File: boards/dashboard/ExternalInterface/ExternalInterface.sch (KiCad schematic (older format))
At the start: 4 parts, among them J1 micromatch_female_TOP_ENTRY_l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, J2 Ampseal_14, J3 micromatch_female_TOP_ENTRY_l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, U1 RJ45_VT

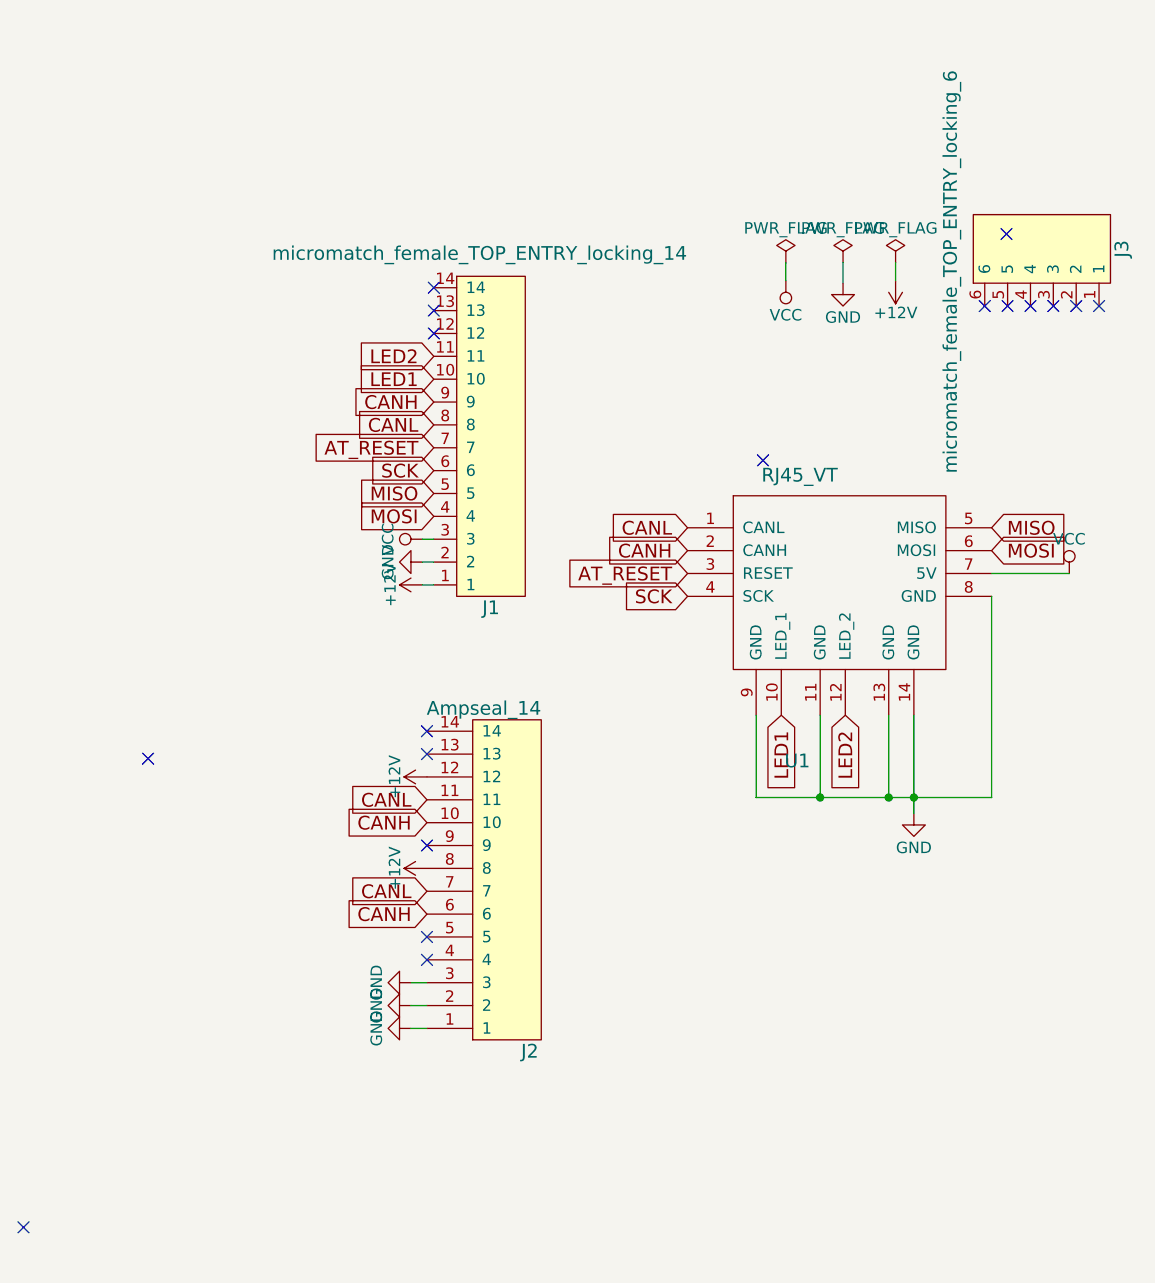
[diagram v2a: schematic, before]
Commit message: Updated External Interface
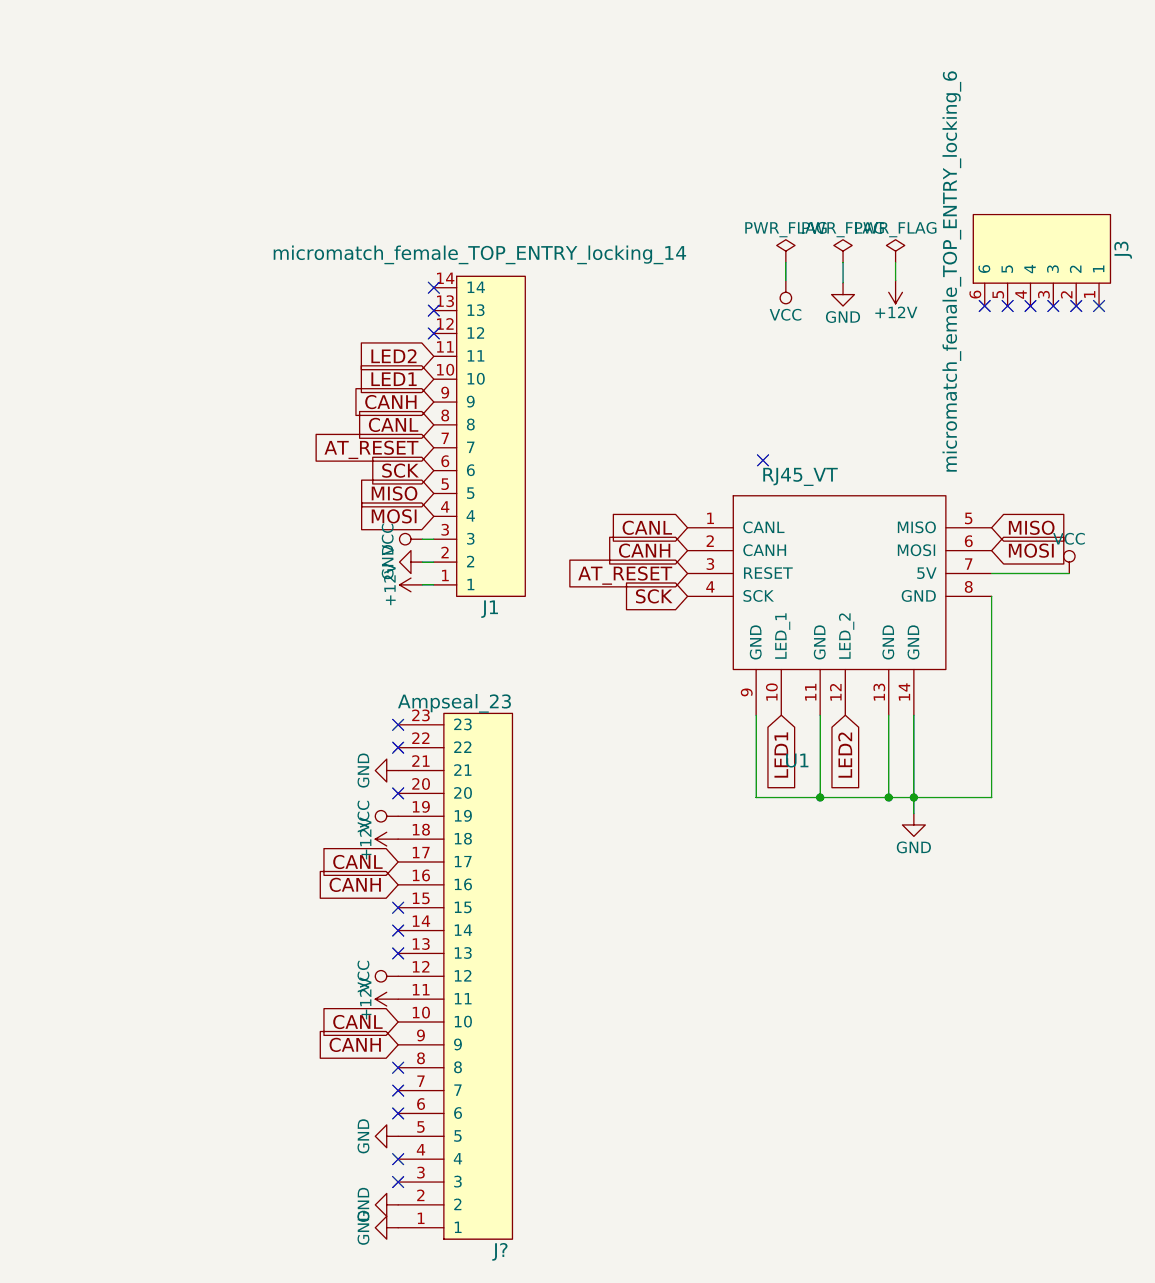
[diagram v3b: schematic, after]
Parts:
- removed J2: Ampseal_14, footprints:Ampseal_14, symbol Ampseal_14
- added J?: Ampseal_23, symbol Ampseal_23
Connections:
- net +12V: now also J?.11, J?.18
- net CANH: now also J?.16, J?.9
- net CANL: now also J?.10, J?.17
- net GND: now also J?.1, J?.2, J?.21, J?.5
- net VCC: now also J?.12, J?.19
- no-connect marks 18 -> 21
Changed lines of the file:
@@
-$EndComp
-$Comp
-L Ampseal_14 J2
-U 1 1 5A64D29C
-P 2180 4340
-F 0 "J2" H 1930 5090 60  0000 C CNN
-F 1 "Ampseal_14" H 1880 3590 60  0000 L CNN
-F 2 "footprints:Ampseal_14" H 1980 4640 60  0001 C CNN
-F 3 "" H 1980 4640 60  0001 C CNN
-	1    2180 4340
-	-1   0    0    1
-$EndComp
-$Comp
-L +12V #PWR010
-U 1 1 5A66323E
-P 1980 4290
-F 0 "#PWR010" H 1980 4140 50  0001 C CNN
-F 1 "+12V" H 1980 4430 50  0000 C CNN
-F 2 "" H 1980 4290 50  0001 C CNN
-F 3 "" H 1980 4290 50  0001 C CNN
-	1    1980 4290
-	0    -1   -1   0
-$EndComp
-Text GLabel 1980 4090 0    60   Input ~ 0
-CANH
-Text GLabel 1980 4490 0    60   Input ~ 0
-CANH
-Text GLabel 1980 3990 0    60   Input ~ 0
-CANL
-Text GLabel 1980 4390 0    60   Input ~ 0
-CANL
-$Comp
-L GND #PWR011
-U 1 1 5A663282
-P 1910 4790
-F 0 "#PWR011" H 1910 4540 50  0001 C CNN
-F 1 "GND" H 1910 4640 50  0000 C CNN
-F 2 "" H 1910 4790 50  0001 C CNN
-F 3 "" H 1910 4790 50  0001 C CNN
-	1    1910 4790
-	0    1    1    0
-$EndComp
-$Comp
-L GND #PWR012
-U 1 1 5A663293
-P 1910 4990
-F 0 "#PWR012" H 1910 4740 50  0001 C CNN
-F 1 "GND" H 1910 4840 50  0000 C CNN
-F 2 "" H 1910 4990 50  0001 C CNN
-F 3 "" H 1910 4990 50  0001 C CNN
-	1    1910 4990
-	0    1    1    0
 $EndComp
 $Comp
@@
 	1    0    0    -1
 $EndComp
-Wire Wire Line
-	2010 2950 1960 2950
-Wire Wire Line
-	2010 2850 1960 2850
-Wire Wire Line
-	2010 3050 1960 3050
-Wire Wire Line
-	3550 1640 3550 1720
-Wire Wire Line
-	3800 1640 3800 1730
-Wire Wire Line
-	4030 1640 4030 1720
-Wire Wire Line
-	1910 4790 1980 4790
-Wire Wire Line
-	1910 4890 1980 4890
-Wire Wire Line
-	1910 4990 1980 4990
 Text GLabel 4450 2800 2    60   Input ~ 0
 MISO
@@
 	1    0    0    -1
 $EndComp
-Wire Wire Line
-	4110 4050 4110 3620
-Wire Wire Line
-	4000 3620 4000 3980
-Wire Wire Line
-	3420 3980 4450 3980
-Connection ~ 4110 3980
-Wire Wire Line
-	3700 3620 3700 3980
-Connection ~ 4000 3980
-Wire Wire Line
-	3420 3620 3420 3980
-Connection ~ 3700 3980
-Wire Wire Line
-	4450 3980 4450 3100
 $Comp
 L VCC #PWR014
@@
 	1    0    0    -1
 $EndComp
-Wire Wire Line
-	4450 3000 4790 3000
 NoConn ~ 2010 1750
 NoConn ~ 2010 1850
@@
 NoConn ~ 4520 1830
 NoConn ~ 4420 1830
-$Comp
-L GND #PWR015
-U 1 1 5A8B7071
-P 1910 4890
-F 0 "#PWR015" H 1910 4640 50  0001 C CNN
-F 1 "GND" H 1910 4740 50  0000 C CNN
-F 2 "" H 1910 4890 50  0001 C CNN
-F 3 "" H 1910 4890 50  0001 C CNN
-	1    1910 4890
-	0    1    1    0
-$EndComp
-$Comp
-L +12V #PWR016
-U 1 1 5A8B721D
-P 1980 3890
-F 0 "#PWR016" H 1980 3740 50  0001 C CNN
-F 1 "+12V" H 1980 4030 50  0000 C CNN
-F 2 "" H 1980 3890 50  0001 C CNN
-F 3 "" H 1980 3890 50  0001 C CNN
-	1    1980 3890
-	0    -1   -1   0
-$EndComp
-NoConn ~ 1980 3790
-NoConn ~ 1980 3690
-NoConn ~ 1980 4190
-NoConn ~ 1980 4690
-NoConn ~ 1980 4590
 NoConn ~ 3450 2505
-NoConn ~ 215  5860
-NoConn ~ 760  3810
-NoConn ~ 4515 1515
+$Comp
+L Ampseal_23 J?
+U 1 1 5AA40700
+P 2054 4762
+F 0 "J?" H 1804 5962 60  0000 C CNN
+F 1 "Ampseal_23" H 1754 3562 60  0000 L CNN
+F 2 "" H 1854 5512 60  0001 C CNN
+F 3 "" H 1854 5512 60  0001 C CNN
+	1    2054 4762
+	-1   0    0    1
+$EndComp
+$Comp
+L GND #PWR?
+U 1 1 5AA408D9
+P 1854 5862
+F 0 "#PWR?" H 1854 5612 50  0001 C CNN
+F 1 "GND" H 1854 5712 50  0000 C CNN
+F 2 "" H 1854 5862 50  0001 C CNN
+F 3 "" H 1854 5862 50  0001 C CNN
+	1    1854 5862
+	0    1    1    0
+$EndComp
+$Comp
+L GND #PWR?
+U 1 1 5AA408F3
+P 1854 5762
+F 0 "#PWR?" H 1854 5512 50  0001 C CNN
+F 1 "GND" H 1854 5612 50  0000 C CNN
+F 2 "" H 1854 5762 50  0001 C CNN
+F 3 "" H 1854 5762 50  0001 C CNN
+	1    1854 5762
+	0    1    1    0
+$EndComp
+$Comp
+L GND #PWR?
+U 1 1 5AA4095E
+P 1854 5462
+F 0 "#PWR?" H 1854 5212 50  0001 C CNN
+F 1 "GND" H 1854 5312 50  0000 C CNN
+F 2 "" H 1854 5462 50  0001 C CNN
+F 3 "" H 1854 5462 50  0001 C CNN
+	1    1854 5462
+	0    1    1    0
+$EndComp
+Text GLabel 1854 5062 0    60   Input ~ 0
+CANH
+Text GLabel 1854 4962 0    60   Input ~ 0
+CANL
+$Comp
+L +12V #PWR?
+U 1 1 5AA4099A
+P 1854 4862
+F 0 "#PWR?" H 1854 4712 50  0001 C CNN
+F 1 "+12V" H 1854 5002 50  0000 C CNN
+F 2 "" H 1854 4862 50  0001 C CNN
+F 3 "" H 1854 4862 50  0001 C CNN
+	1    1854 4862
+	0    -1   -1   0
+$EndComp
+$Comp
+L VCC #PWR?
+U 1 1 5AA409B4
+P 1854 4762
+F 0 "#PWR?" H 1854 4612 50  0001 C CNN
+F 1 "VCC" H 1854 4912 50  0000 C CNN
+F 2 "" H 1854 4762 50  0001 C CNN
+F 3 "" H 1854 4762 50  0001 C CNN
+	1    1854 4762
+	0    -1   -1   0
+$EndComp
+Text GLabel 1854 4362 0    60   Input ~ 0
+CANH
+Text GLabel 1854 4262 0    60   Input ~ 0
+CANL
+$Comp
+L +12V #PWR?
+U 1 1 5AA409F0
+P 1854 4162
+F 0 "#PWR?" H 1854 4012 50  0001 C CNN
+F 1 "+12V" H 1854 4302 50  0000 C CNN
+F 2 "" H 1854 4162 50  0001 C CNN
+F 3 "" H 1854 4162 50  0001 C CNN
+	1    1854 4162
+	0    -1   -1   0
+$EndComp
+$Comp
+L VCC #PWR?
+U 1 1 5AA40A32
+P 1854 4062
+F 0 "#PWR?" H 1854 3912 50  0001 C CNN
+F 1 "VCC" H 1854 4212 50  0000 C CNN
+F 2 "" H 1854 4062 50  0001 C CNN
+F 3 "" H 1854 4062 50  0001 C CNN
+	1    1854 4062
+	0    -1   -1   0
+$EndComp
+$Comp
+L GND #PWR?
+U 1 1 5AA40A4C
+P 1854 3862
+F 0 "#PWR?" H 1854 3612 50  0001 C CNN
+F 1 "GND" H 1854 3712 50  0000 C CNN
+F 2 "" H 1854 3862 50  0001 C CNN
+F 3 "" H 1854 3862 50  0001 C CNN
+	1    1854 3862
+	0    1    1    0
+$EndComp
+Wire Wire Line
+	2010 2950 1960 2950
+Wire Wire Line
+	2010 2850 1960 2850
+Wire Wire Line
+	2010 3050 1960 3050
+Wire Wire Line
+	3550 1640 3550 1720
+Wire Wire Line
+	3800 1640 3800 1730
+Wire Wire Line
+	4030 1640 4030 1720
+Wire Wire Line
+	4110 4050 4110 3620
+Wire Wire Line
+	4000 3620 4000 3980
+Wire Wire Line
+	3420 3980 4450 3980
+Connection ~ 4110 3980
+Wire Wire Line
+	3700 3620 3700 3980
+Connection ~ 4000 3980
+Wire Wire Line
+	3420 3620 3420 3980
+Connection ~ 3700 3980
+Wire Wire Line
+	4450 3980 4450 3100
+Wire Wire Line
+	4450 3000 4790 3000
+NoConn ~ 1854 3762
+NoConn ~ 1854 3662
+NoConn ~ 1854 3962
+NoConn ~ 1854 4462
+NoConn ~ 1854 4562
+NoConn ~ 1854 4662
+NoConn ~ 1854 5162
+NoConn ~ 1854 5262
+NoConn ~ 1854 5362
+NoConn ~ 1854 5562
+NoConn ~ 1854 5662
 $EndSCHEMATC
